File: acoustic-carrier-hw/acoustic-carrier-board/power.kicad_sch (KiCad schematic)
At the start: 65 parts, among them J2 Conn_02x08_Odd_Even, Q2 AO3401A, U17 TPS2121RUX, U19 TLV62569DBV, U21 TLV62569DBV, U24 TLV62569DBV, U25 TLV62569DBV, U26 OPA376xxDBV

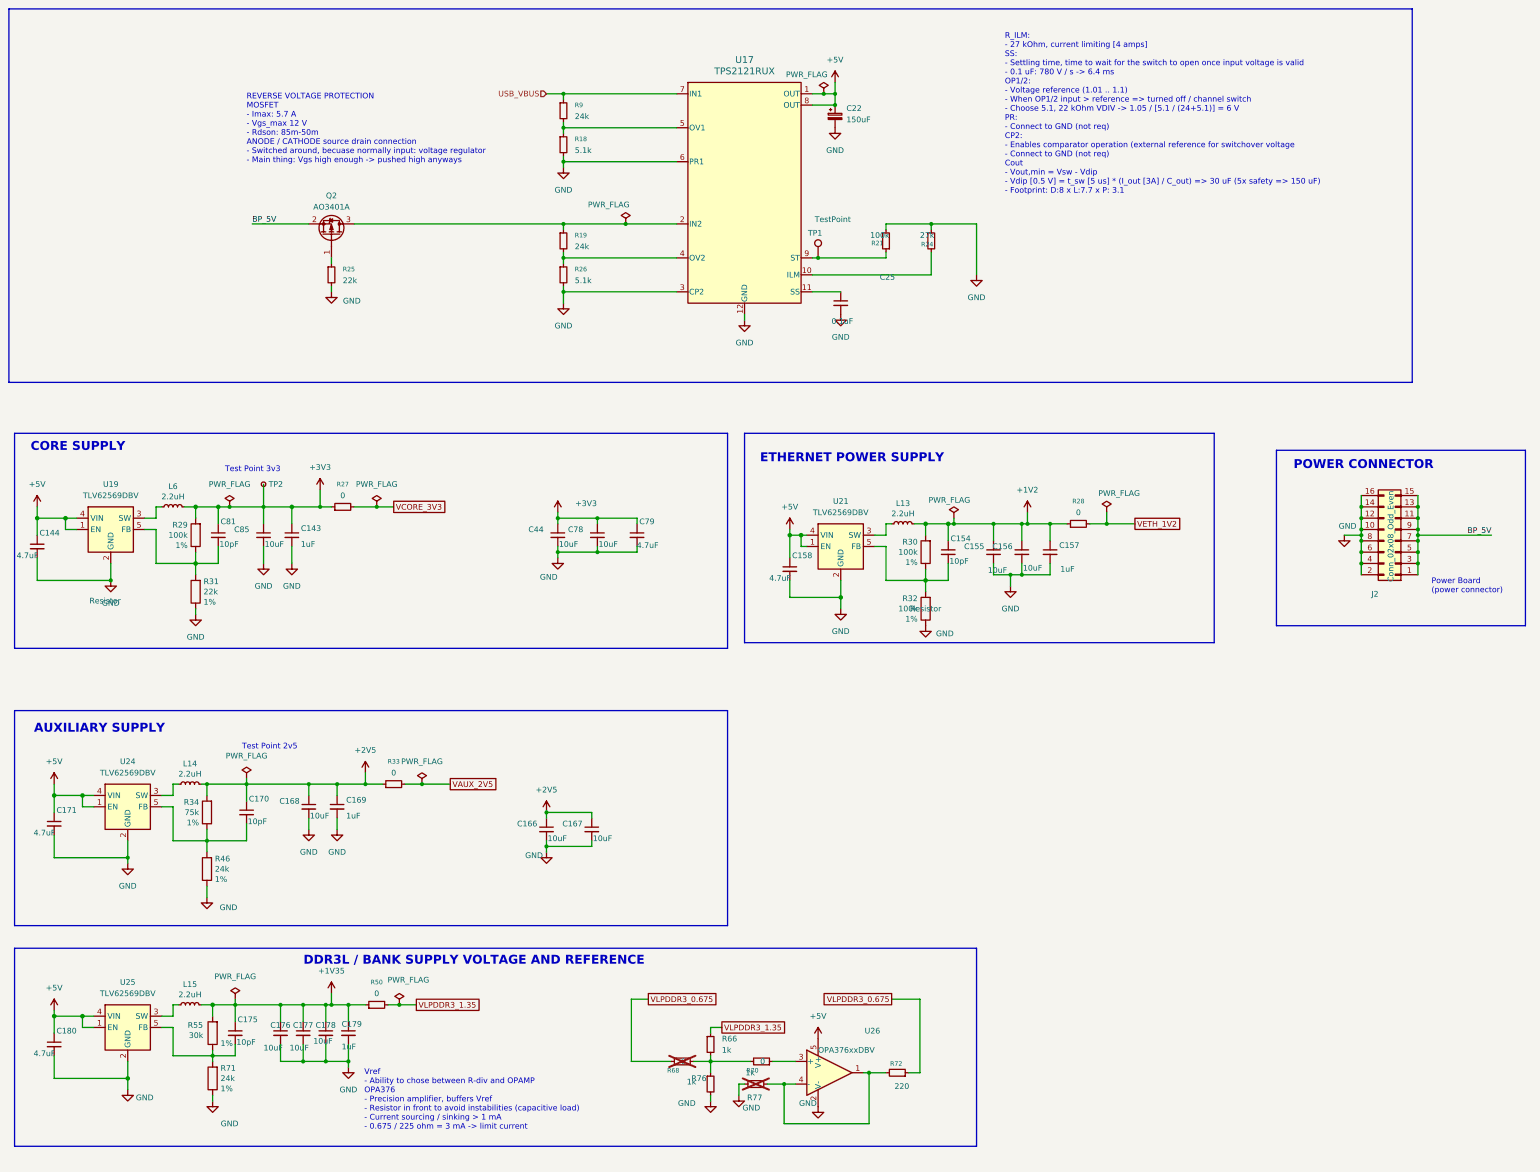
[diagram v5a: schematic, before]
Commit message: [¢arrier] Did major cchecks of ETH, DDR, ANALOG, config (next) check buffer circuit driven by USB-CC, then start layout
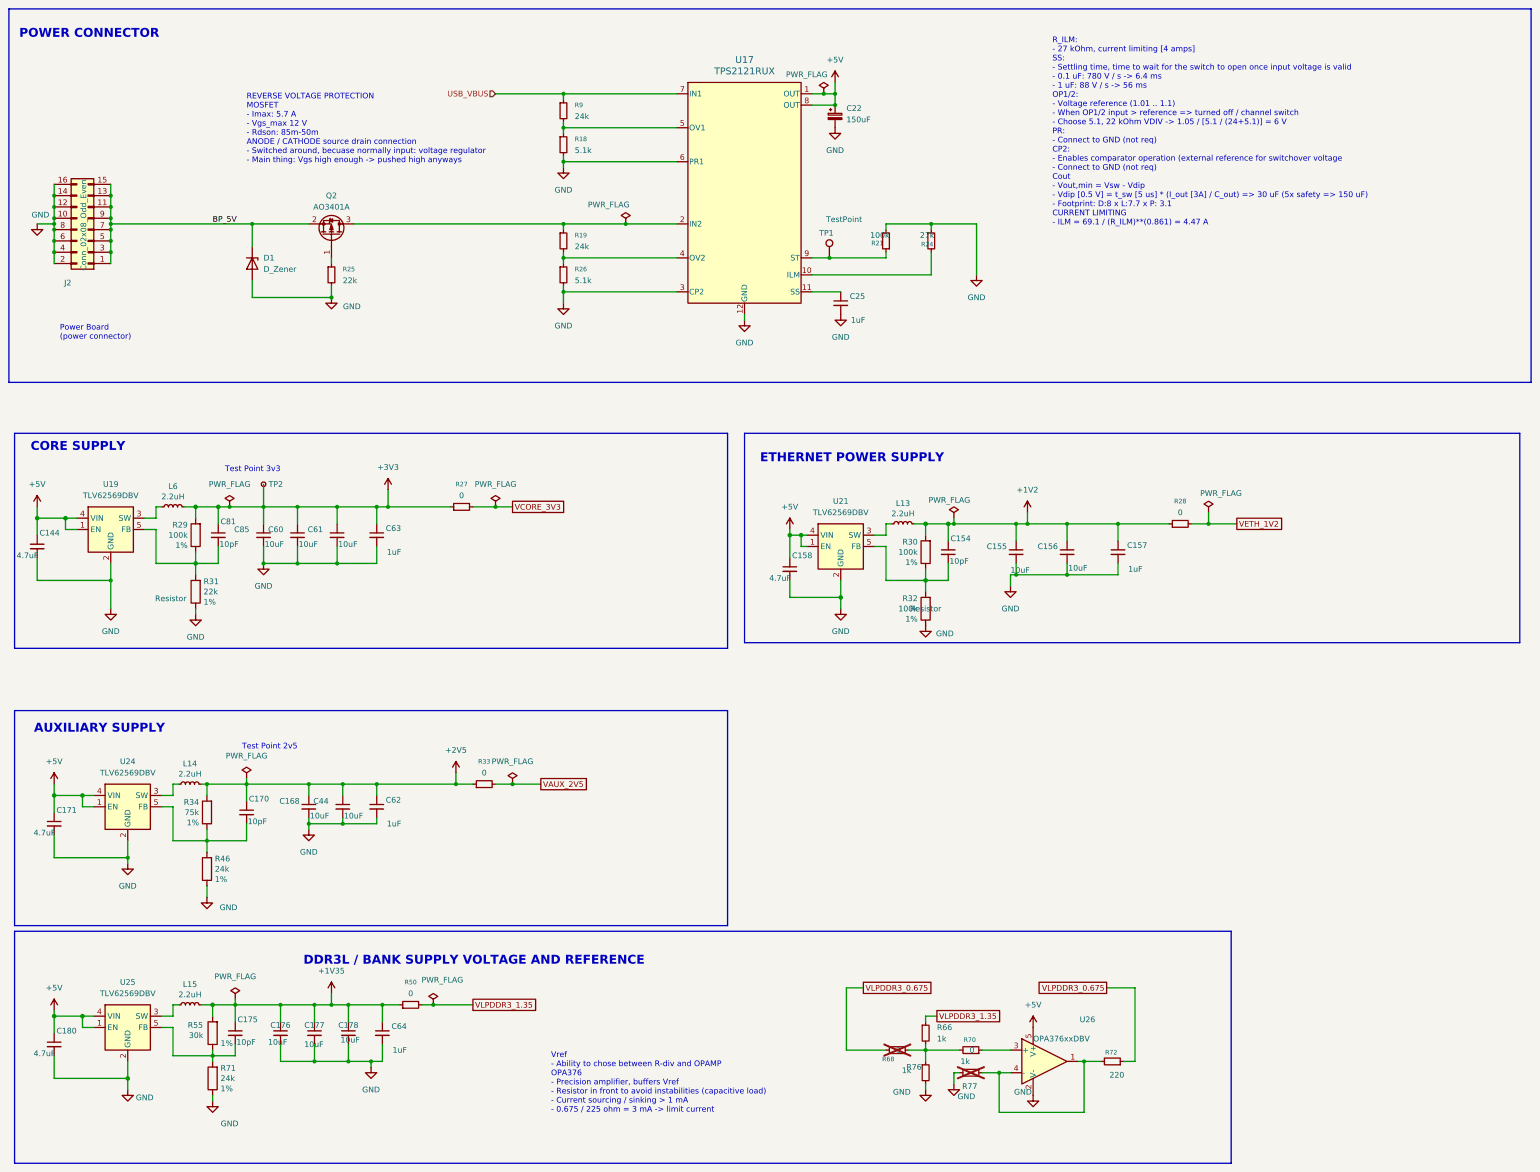
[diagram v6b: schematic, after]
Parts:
- removed C143, C169, C179: 1uF, Capacitor_SMD:C_0805_2012Metric, symbol Device:C_Small
- removed C166, C167, C78: 10uF, Capacitor_SMD:C_0603_1608Metric, symbol Device:C_Small
- removed C79: 4.7uF, Capacitor_SMD:C_0402_1005Metric, symbol Device:C_Small
- added C60, C61: 10uF, Capacitor_SMD:C_0603_1608Metric, symbol Device:C_Small
- added C62, C63, C64: 1uF, Capacitor_SMD:C_0805_2012Metric, symbol Device:C_Small
- added D1: D_Zener, Diode_SMD:D_SOD-323_HandSoldering, symbol Device:D_Zener
- C25: value 0.1uF -> 1uF; footprint Capacitor_SMD:C_0402_1005Metric -> Capacitor_SMD:C_0805_2012Metric; LPN C307331 -> C28323; MPN CL05B104KB54PNC -> CL21B105KBFNNNE
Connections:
- net +1V35: now also C64.1
- net +2V5: now also C44.1, C62.1
- net +3V3: now also C60.1, C61.1, C63.1; no longer C44.1
- net BP_5V: now also D1.1 (K)
- net GND: now also C60.2, C61.2, C62.2, C63.2, C64.2, D1.2 (A)
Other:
- note added: "R_ILM: - 27 kOhm, current limiting [4 amps] SS: - Settling time, time to wait for the switch to open once input voltage is valid - 0.1 uF: 780 V / s -> 6.4 ms - 1 uF: 88 V / s -> 56 ms OP1/2: - Voltage reference (1.01 .. 1.1) - When OP1/2 input > reference => turned off / channel switch - Choose 5.1, 22 kOhm VDIV -> 1.05 / [5.1 / (24+5.1)] = 6 V PR: - Connect to GND (not req) CP2: - Enables compa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"
- note removed: "R_ILM: - 27 kOhm, current limiting [4 amps] SS: - Settling time, time to wait for the switch to open once input voltage is valid - 0.1 uF: 780 V / s -> 6.4 ms OP1/2: - Voltage reference (1.01 .. 1.1) - When OP1/2 input > reference => turned off / channel switch - Choose 5.1, 22 kOhm VDIV -> 1.05 / [5.1 / (24+5.1)] = 6 V PR: - Connect to GND (not req) CP2: - Enables comparator operation (external 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"
- moved on the sheet: C155, C156, C157, C177, C178, J2, R27, R28, R33, R50, R66, R68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

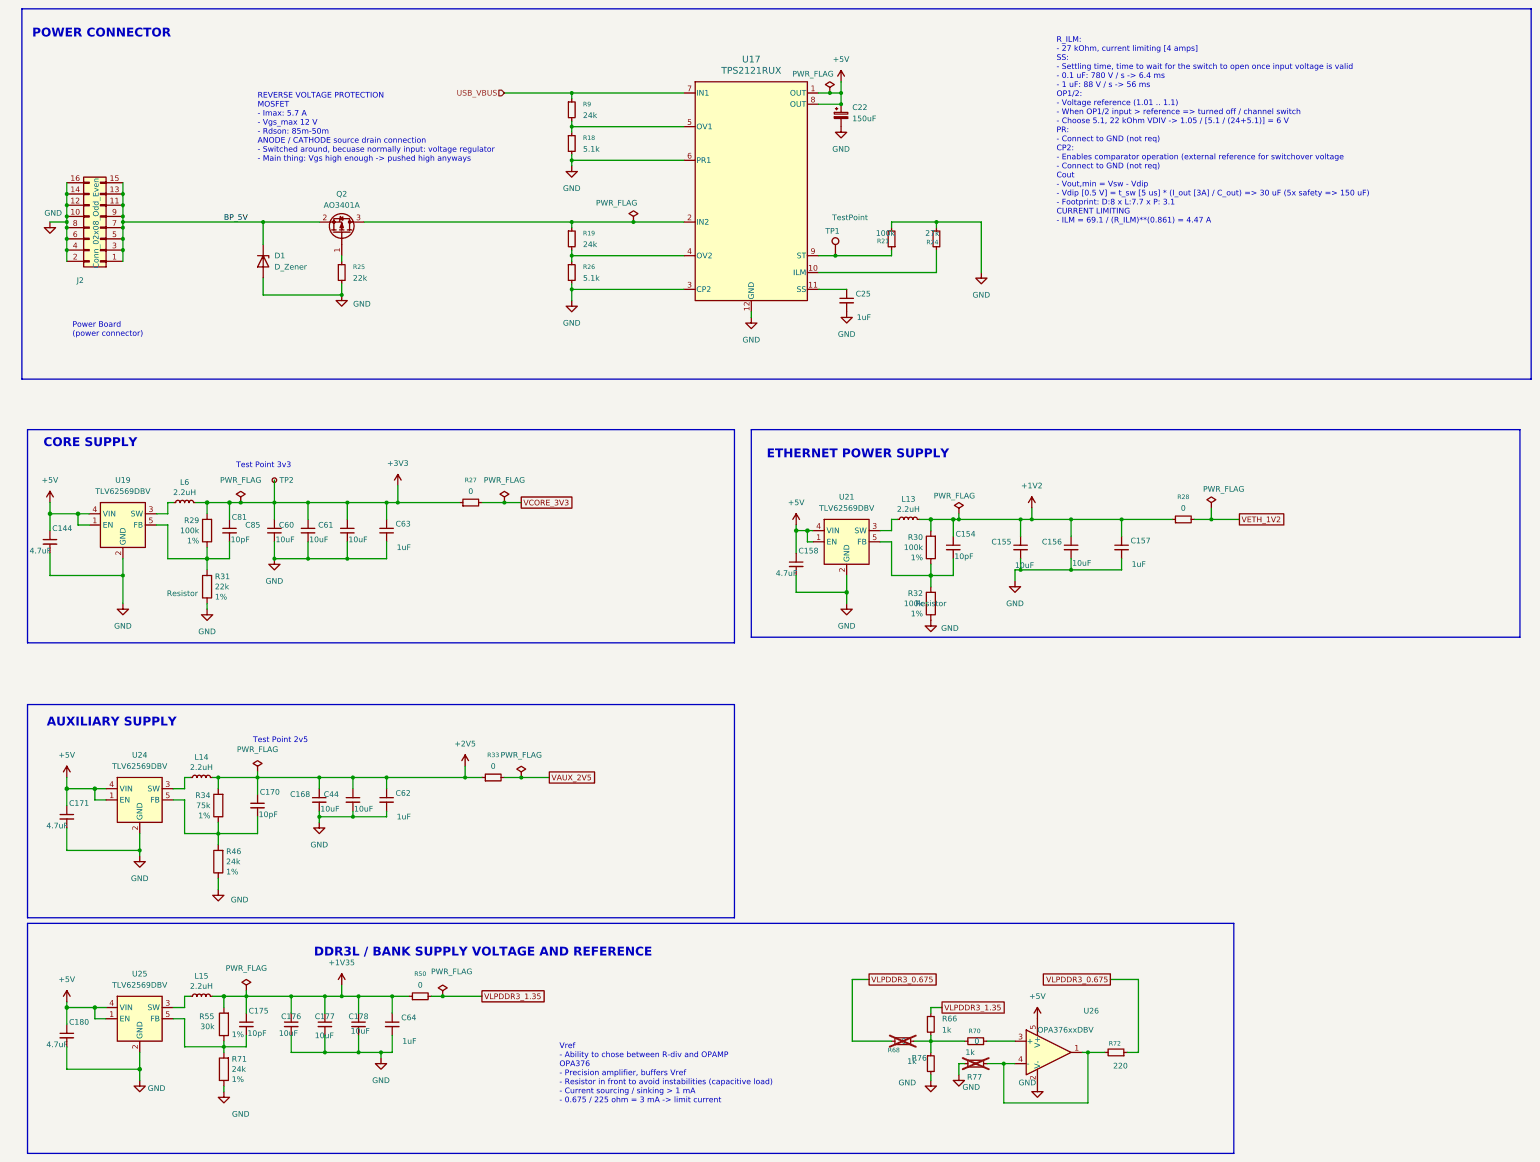
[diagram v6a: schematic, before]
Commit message: [carrier] Added testpoints
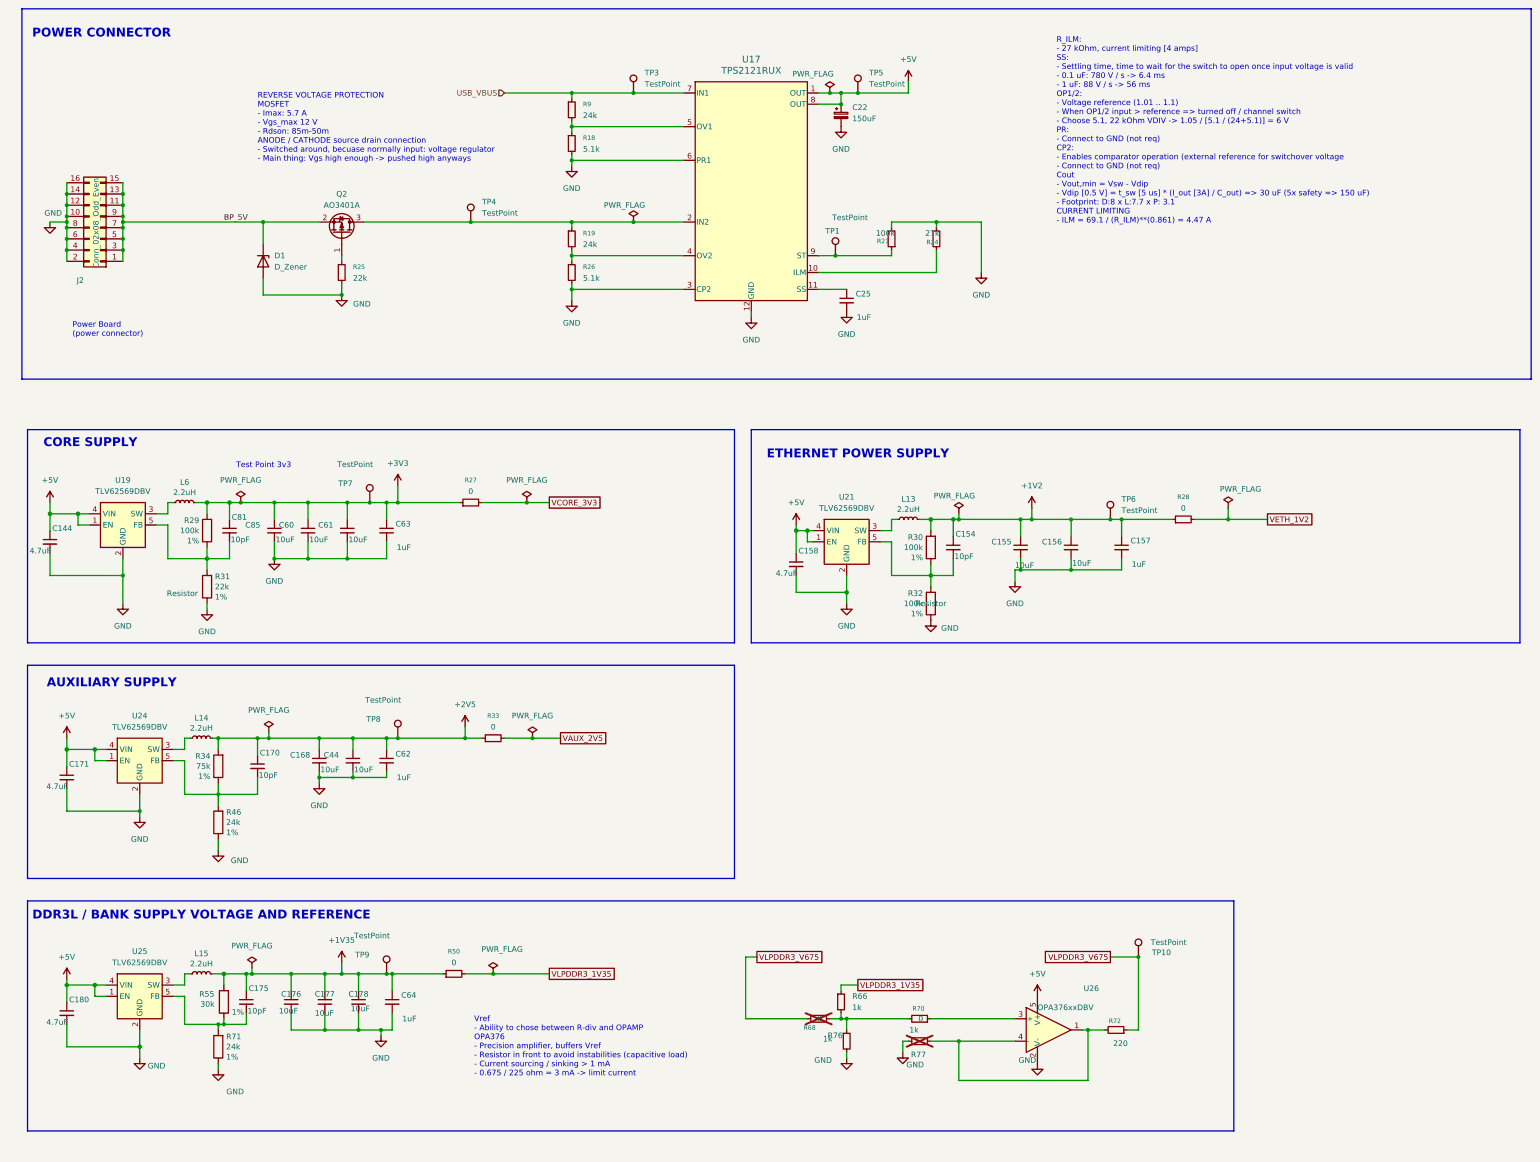
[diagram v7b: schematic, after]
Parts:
- removed TP2: TestPoint_Small, TestPoint:TestPoint_Pad_D1.5mm, symbol Connector:TestPoint_Small
- added TP10, TP3, TP4, TP5, TP6, TP7, TP8, TP9: TestPoint, TestPoint:TestPoint_Loop_D1.80mm_Drill1.0mm_Beaded, symbol Connector:TestPoint
- R29, R30, R32: footprint Resistor_SMD:R_0402_1005Metric -> Resistor_SMD:R_0603_1608Metric
- R66, R76: LPN 0603WAF1001T5E -> C21190; MPN C21190 -> 0603WAF1001T5E
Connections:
- net +1V2: now also TP6.1
- net +1V35: now also TP9.1
- net +2V5: now also TP8.1
- net +3V3: now also TP7.1
- net +5V: now also TP5.1
- net USB_VBUS: now also TP3.1
- net at Q2.3 (D), R19.1, U17.2 (IN2): now also TP4.1
- net VLPDDR3_0.675 renamed VLPDDR3_V675
- net VLPDDR3_V675: now also TP10.1
- net VLPDDR3_1.35 renamed VLPDDR3_1V35
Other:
- note removed: "Test Point 2v5"
- moved on the sheet: C168, C170, C171, C175, C176, C177, C178, C180, C44, C62, C64, L14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
